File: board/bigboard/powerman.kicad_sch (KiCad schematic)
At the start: 11 parts, among them J1 Conn_02x02_Row_Letter_First, J2 Conn_02x02_Row_Letter_First

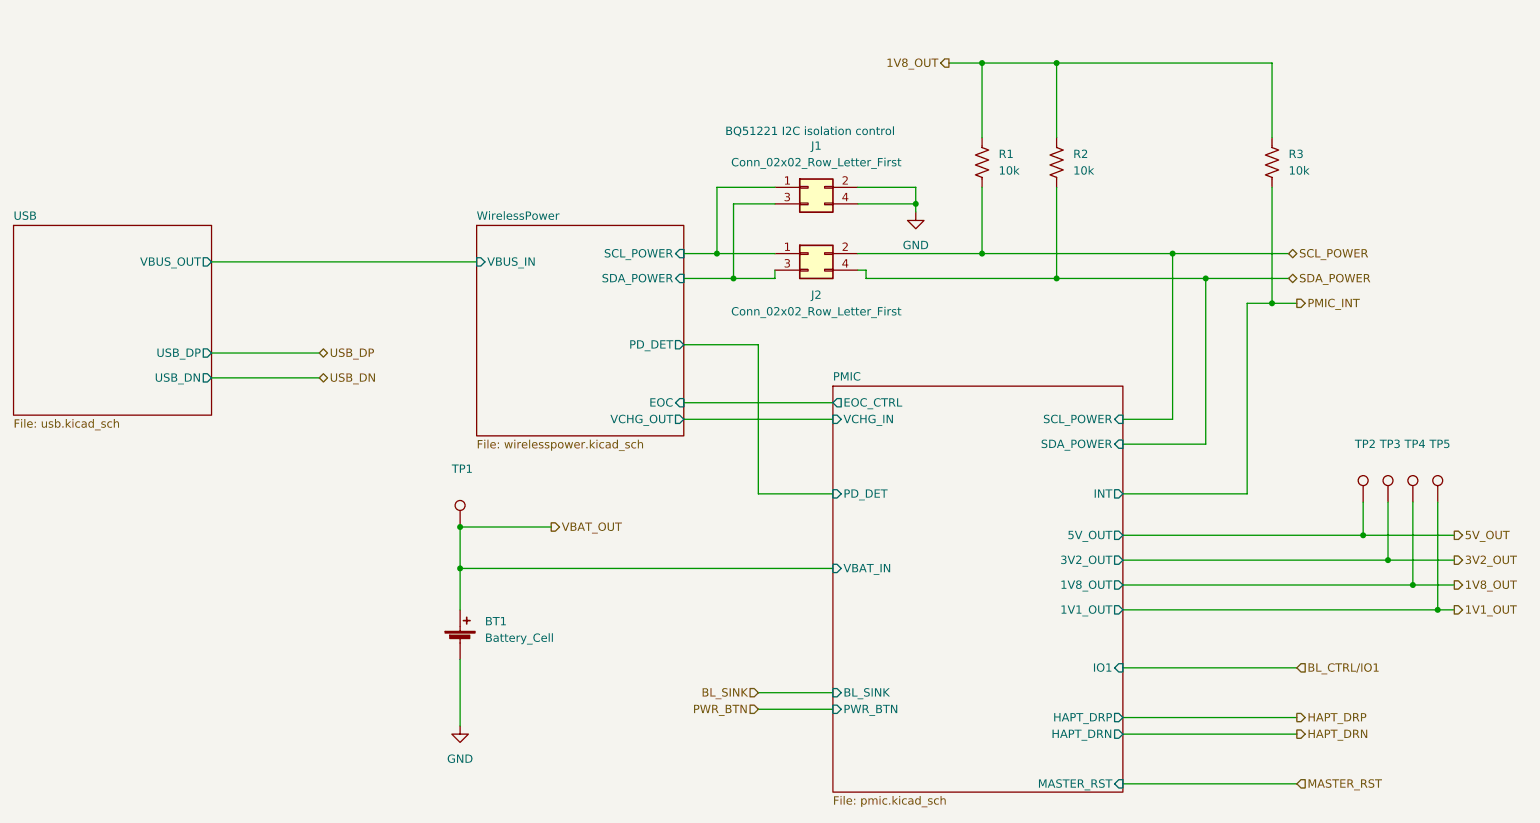
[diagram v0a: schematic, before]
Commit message: Manufactured version of bigboard
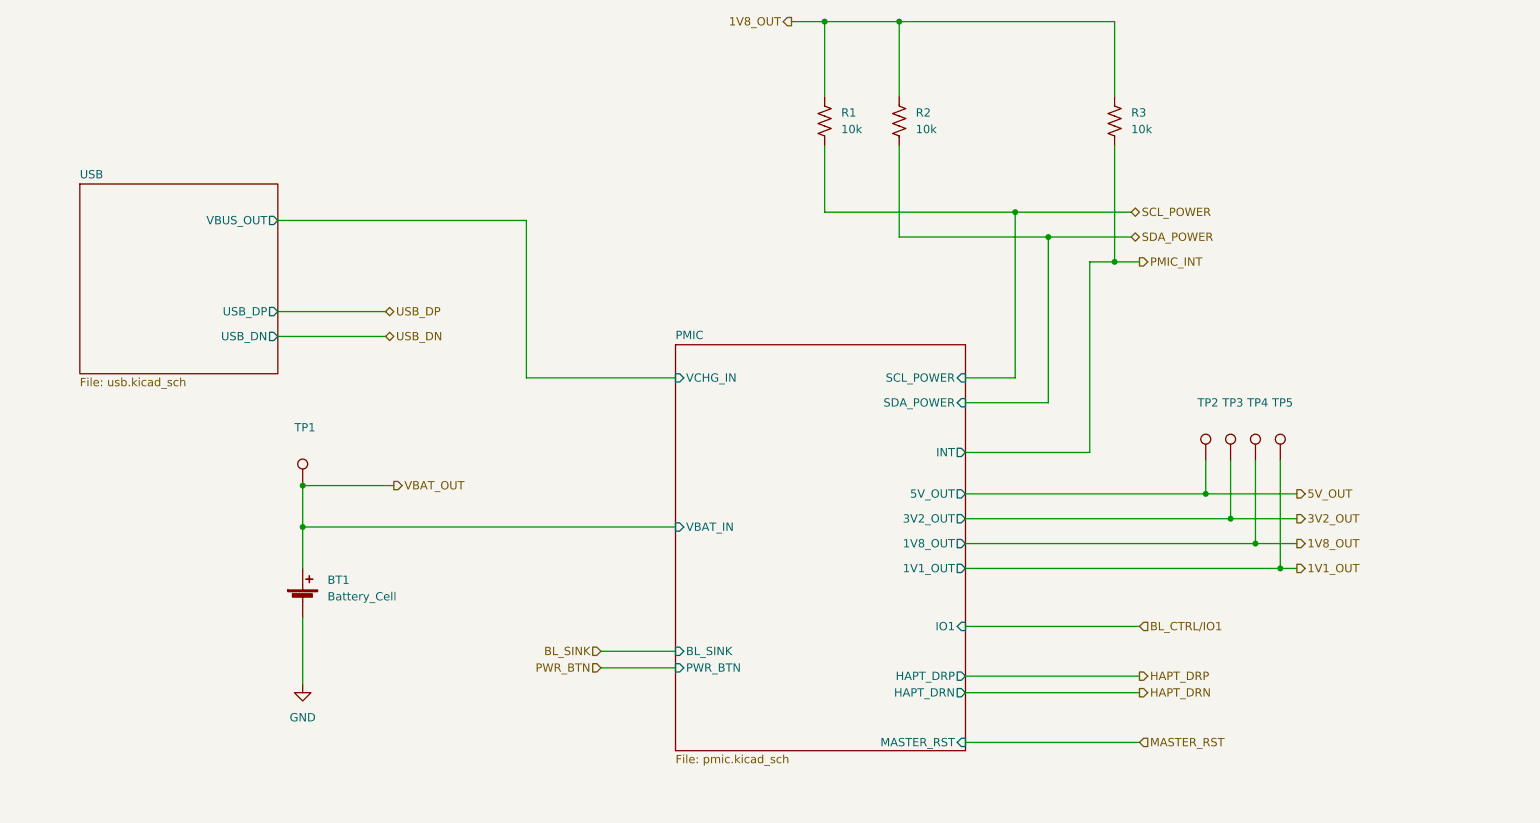
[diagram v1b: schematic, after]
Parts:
- removed J1, J2: Conn_02x02_Row_Letter_First, Connector_PinHeader_2.54mm:PinHeader_2x02_P2.54mm_Vertical, symbol Connector_Generic:Conn_02x02_Odd_Even
- R1, R2, R3: MPN (none) -> RC0201FR-0710KL
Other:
- removed sheet WirelessPower
- sheet PMIC ports: added none; removed EOC_CTRL, PD_DET
- note removed: "BQ51221 I2C isolation control"
- moved on the sheet: BT1, R1, R2, R3, TP1, TP2, TP3, TP4, TP5
